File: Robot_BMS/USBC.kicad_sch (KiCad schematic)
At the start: 20 parts, among them IC3 AP33772DKZ-13, J1 632723300011, Q5 NDT3055L, Q6 NDT3055L

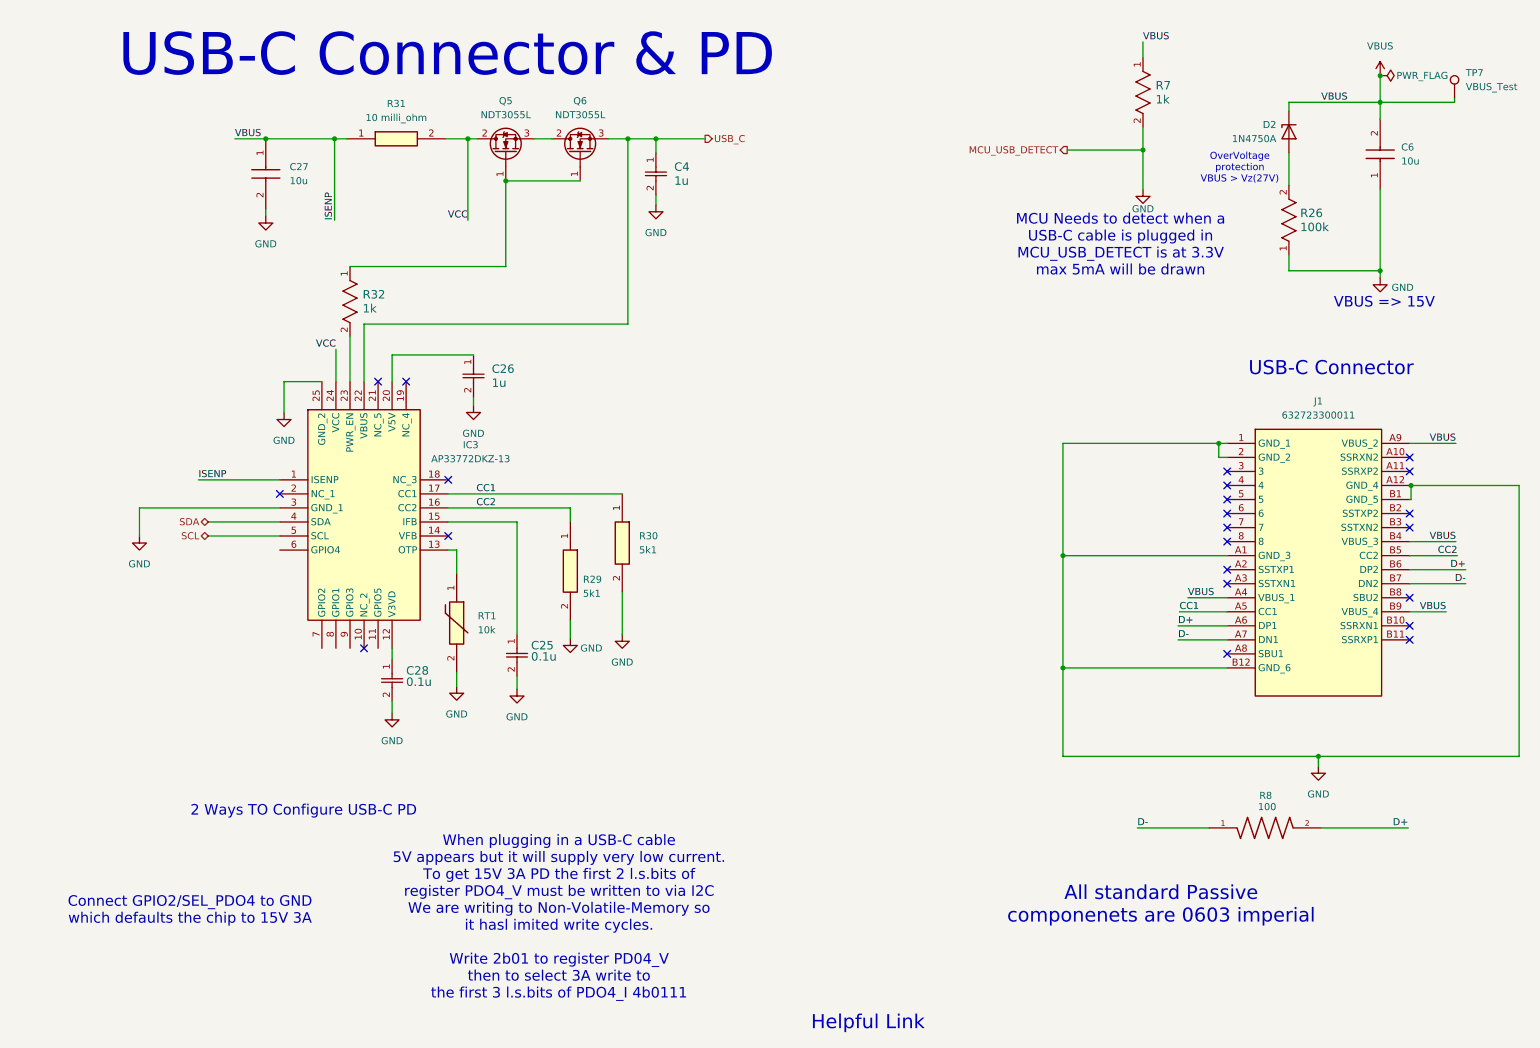
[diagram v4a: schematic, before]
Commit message: placed connectors for BMS PCB
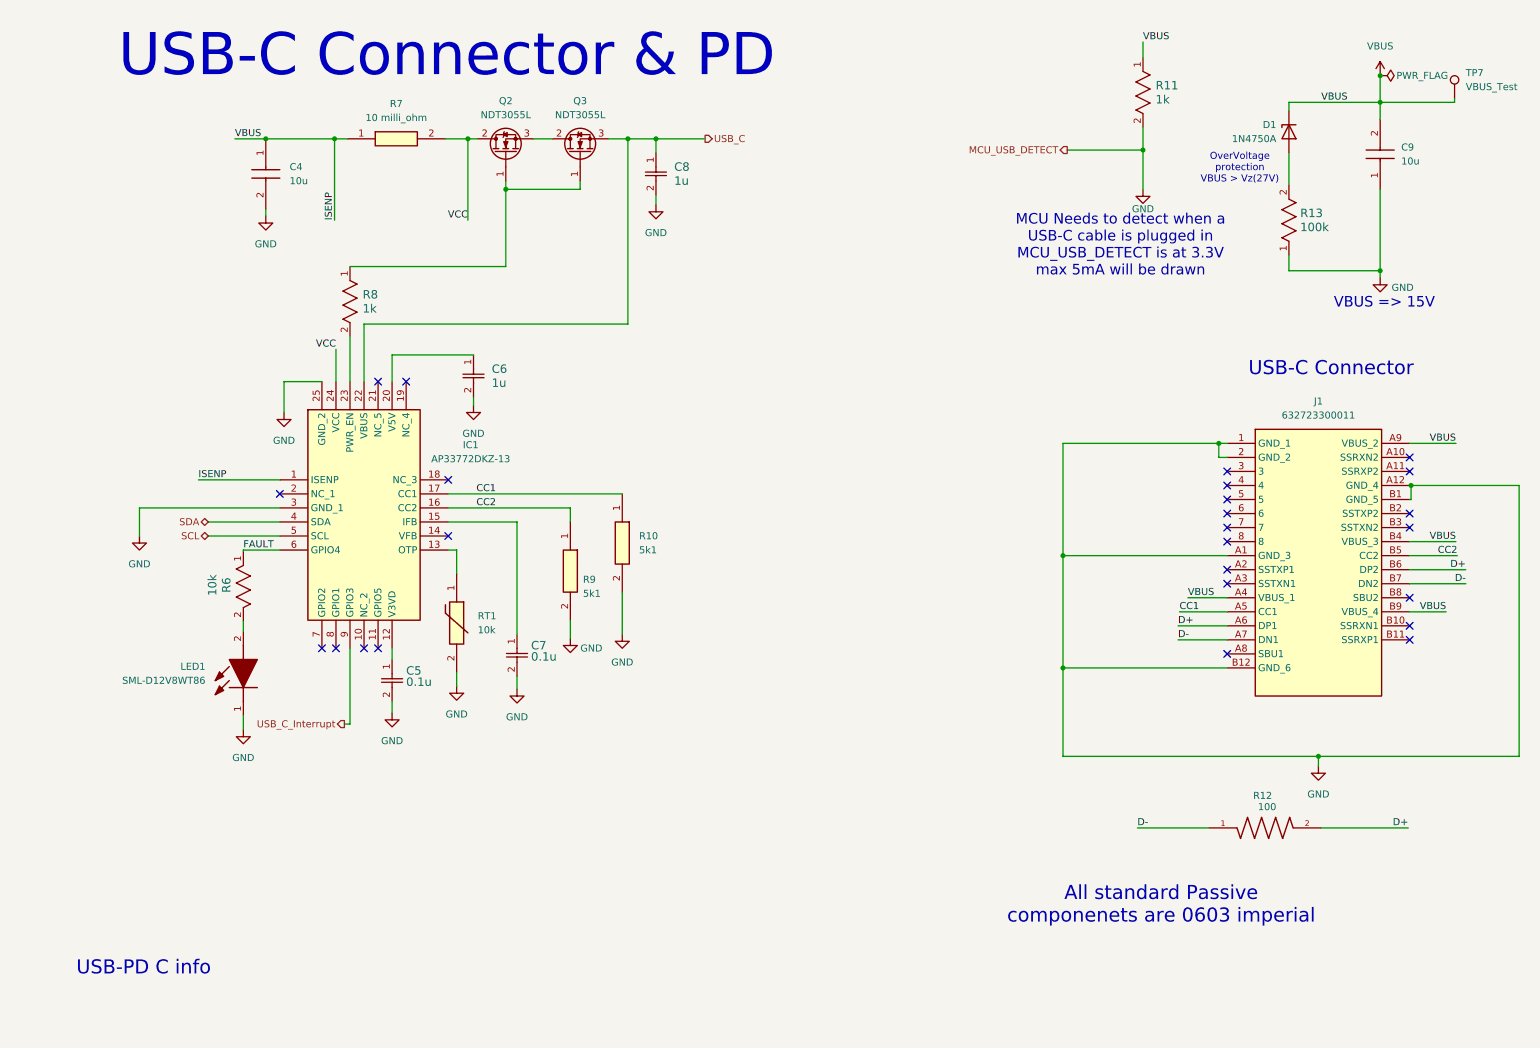
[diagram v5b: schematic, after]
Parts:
- added LED1: SML-D12V8WT86, RobotBMS:SMLD12V8WT86, symbol SML-D12V8WT86:SML-D12V8WT86
- added R6: 10k, RobotBMS:RC0603N_YAG, symbol RC0603FR-0710KL:RC0603FR-0710KL
- IC1: renamed from IC3; footprint QFN50P400X400X80-25N-D -> RobotBMS:QFN50P400X400X80-25N-D
- R10: renamed from R30; footprint ERA3AEB101V -> RobotBMS:ERA3AEB101V
- R7: renamed from R31; footprint RESC1608X60N -> RobotBMS:RESC1608X60N
- R9: renamed from R29; footprint ERA3AEB101V -> RobotBMS:ERA3AEB101V
- RT1: footprint THRMC0603X33N -> RobotBMS:THRMC0603X33N
- renumbered C27 to C4, C28 to C5, C26 to C6, C25 to C7, C4 to C8, C6 to C9, D2 to D1, Q5 to Q2, Q6 to Q3, R7 to R11, R8 to R12, R26 to R13, R32 to R8
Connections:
- net GND: now also LED1.1 (K)
- net FAULT: now reaches IC1.6 (GPIO4)
- net FAULT: now also R6.1
- net USB_C_Interrupt: now reaches IC1.9 (GPIO3)
- new net: LED1.2 (A), R6.2
- no-connect marks 22 -> 25
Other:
- note added: "USB-PD C info"
- note removed: "2 Ways TO Configure USB-C PD"
- note removed: "Connect GPIO2/SEL_PDO4 to GND which defaults the chip to 15V 3A"
- note removed: "Helpful Link"
- note removed: "When plugging in a USB-C cable 5V appears but it will supply very low current. To get 15V 3A PD the first 2 l.s.bits of register PDO4_V must be written to via I2C We are writing to Non-Volatile-Memory so it hasl imited write cycles. Write 2b01 to register PD04_V then to select 3A write to the first 3 l.s.bits of PDO4_I 4b0111"

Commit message: PCB layout up to charging circuit
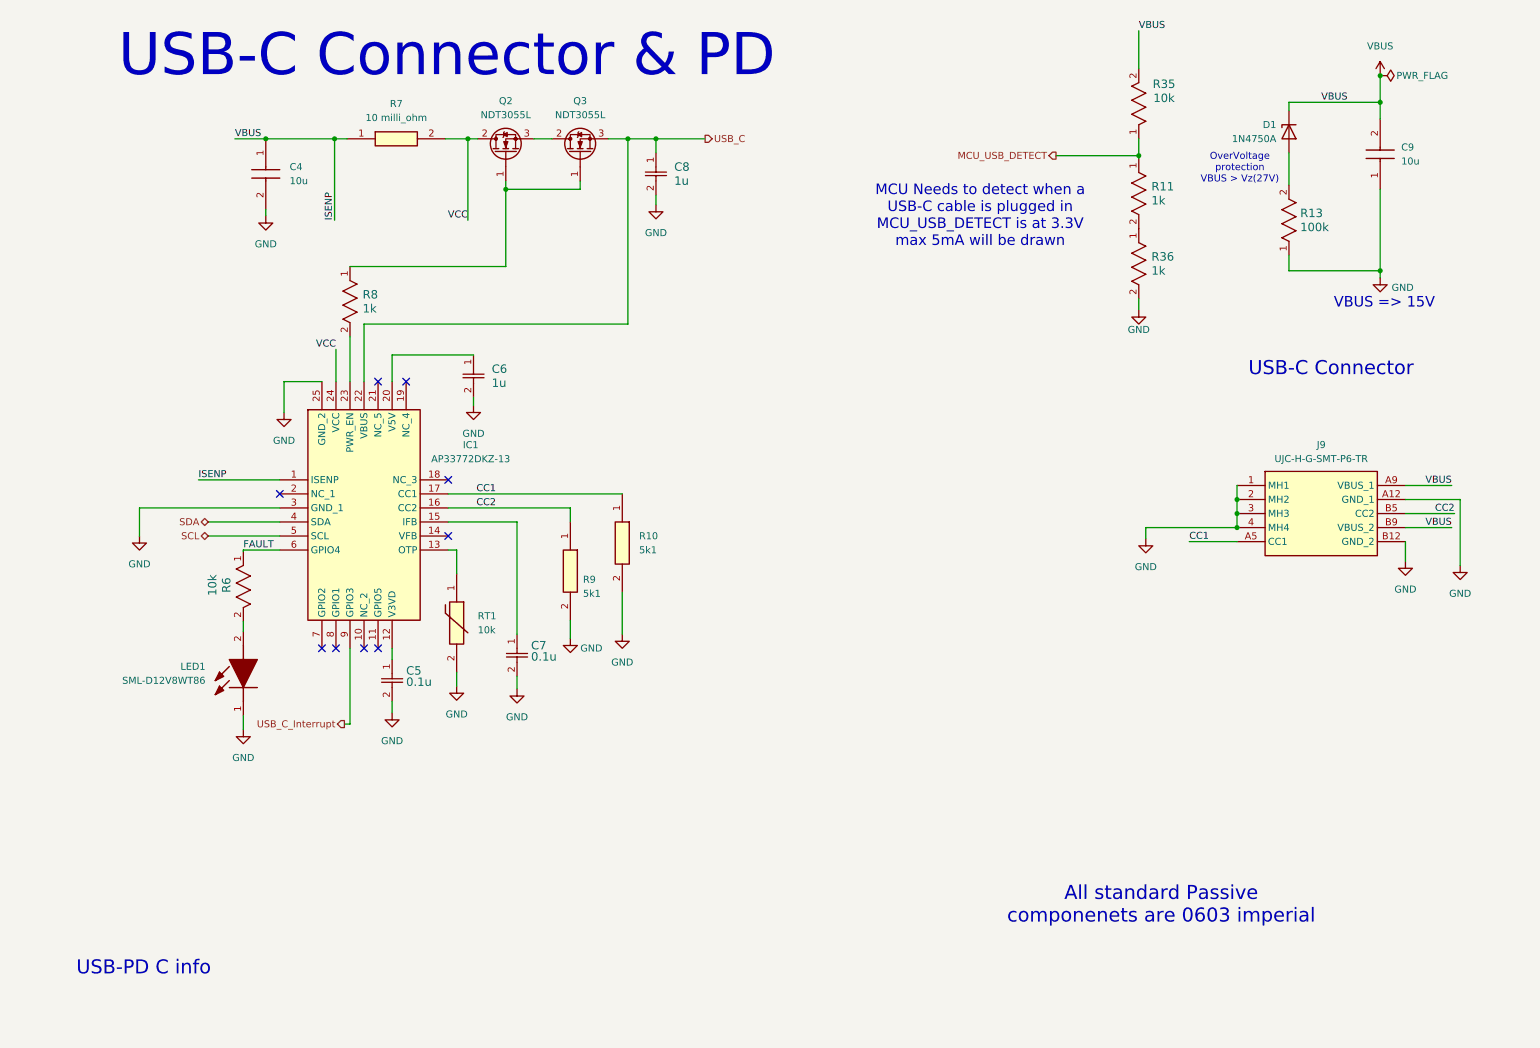
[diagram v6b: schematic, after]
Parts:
- removed J1: 632723300011, RobotBMS:632723300011, symbol USB-C Connector 632723300011:632723300011
- removed R12: 100, RobotBMS:RESC1608X55N, symbol AT0603DRE07100RL:AT0603DRE07100RL
- removed TP7: VBUS_Test, TestPoint:TestPoint_Pad_D4.0mm, symbol Connector:TestPoint
- added J9: UJC-H-G-SMT-P6-TR, UJCHGSMT2P6TR, symbol UJC-H-G-SMT-2-P6-TR USB - C Connector:UJC-H-G-SMT-2-P6-TR
- added R35: 10k, RobotBMS:RC0603N_YAG, symbol RC0603FR-0710KL:RC0603FR-0710KL
- added R36: 1k, RobotBMS:RES_V0603_VIS, symbol CRCW06031K00JNEAIF:CRCW06031K00JNEAIF
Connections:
- net CC1: now also J9.A5 (CC1)
- net CC2: now also J9.B5 (CC2)
- net GND: now also J9.1 (MH1), J9.2 (MH2), J9.3 (MH3), J9.4 (MH4), J9.A12 (GND_1), J9.B12 (GND_2), R36.2; no longer R11.2
- net VBUS: now also J9.A9 (VBUS_1), J9.B9 (VBUS_2), R35.2; no longer R11.1
- new net: R11.2, R36.1
- new net MCU_USB_DETECT: R11.1, R35.1
- no-connect marks 25 -> 9
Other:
- moved on the sheet: R11

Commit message: halfway throgh battery management pcb layout
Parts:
- NTC1: renamed from RT1; value 10k -> 10000
- renumbered J9 to J1, R35 to R11, R11 to R12, R36 to R13, R13 to R14
